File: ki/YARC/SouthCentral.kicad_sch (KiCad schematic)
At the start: 14 parts

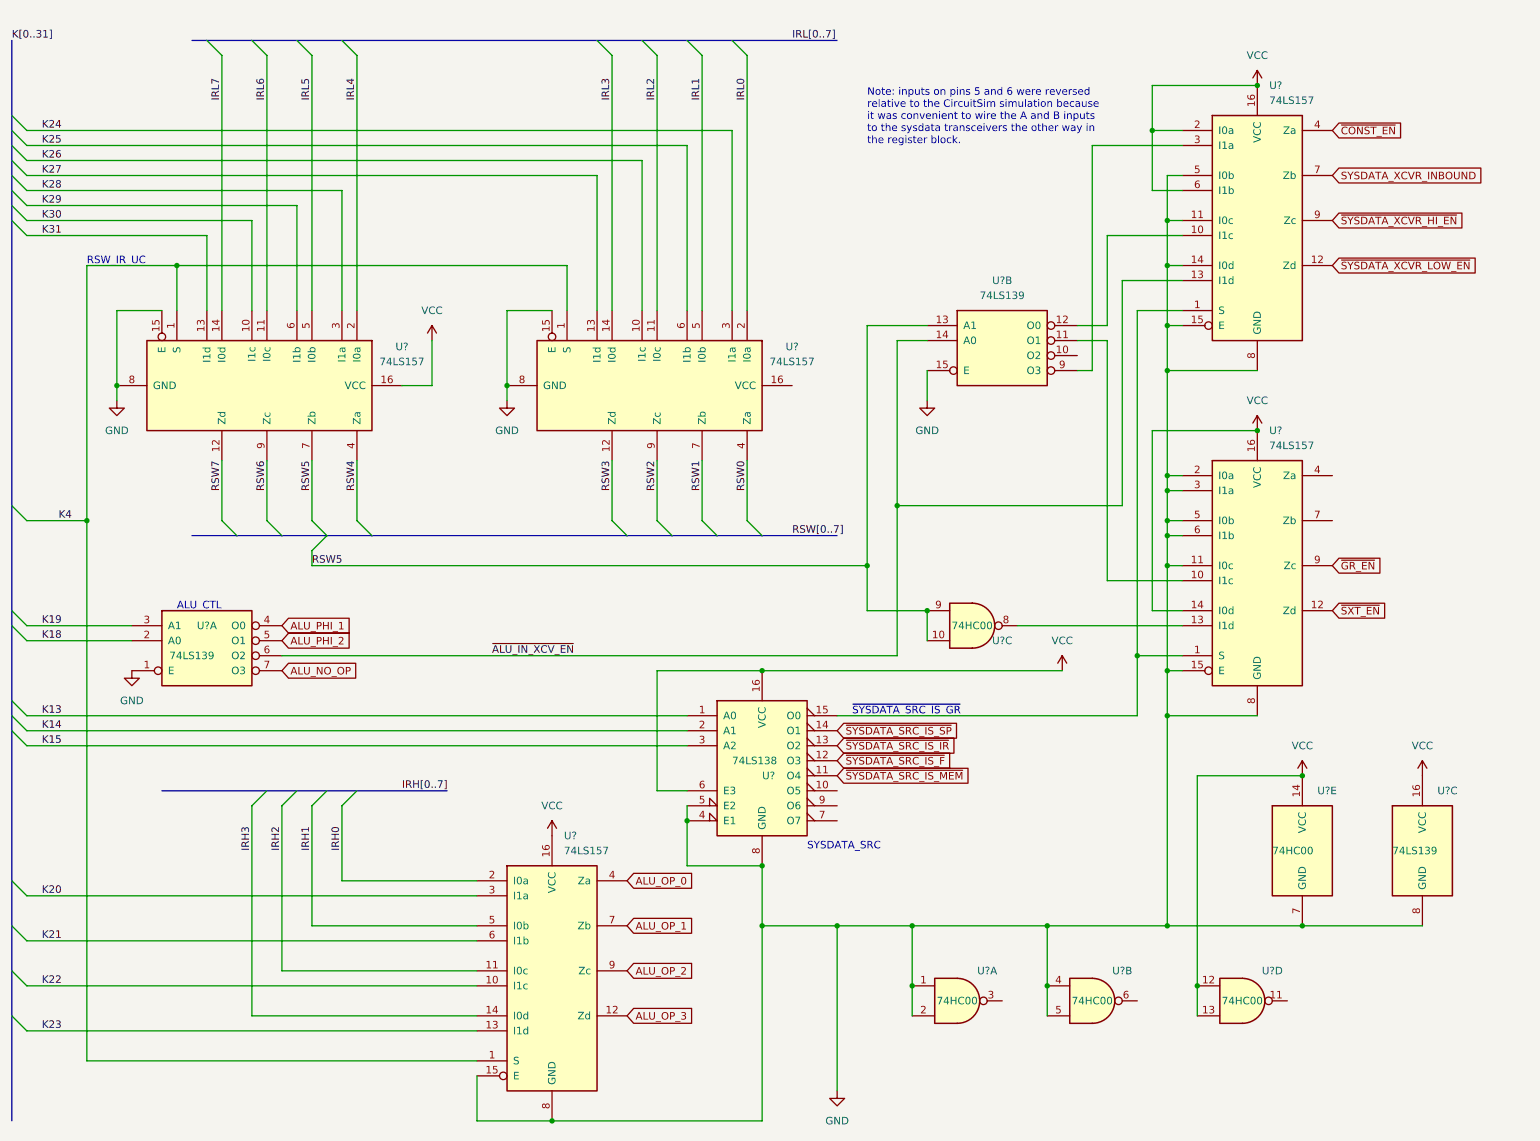
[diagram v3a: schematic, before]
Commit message: Assign part labels (U-numbers) in KiCad and start adding them to Fritzing layouts
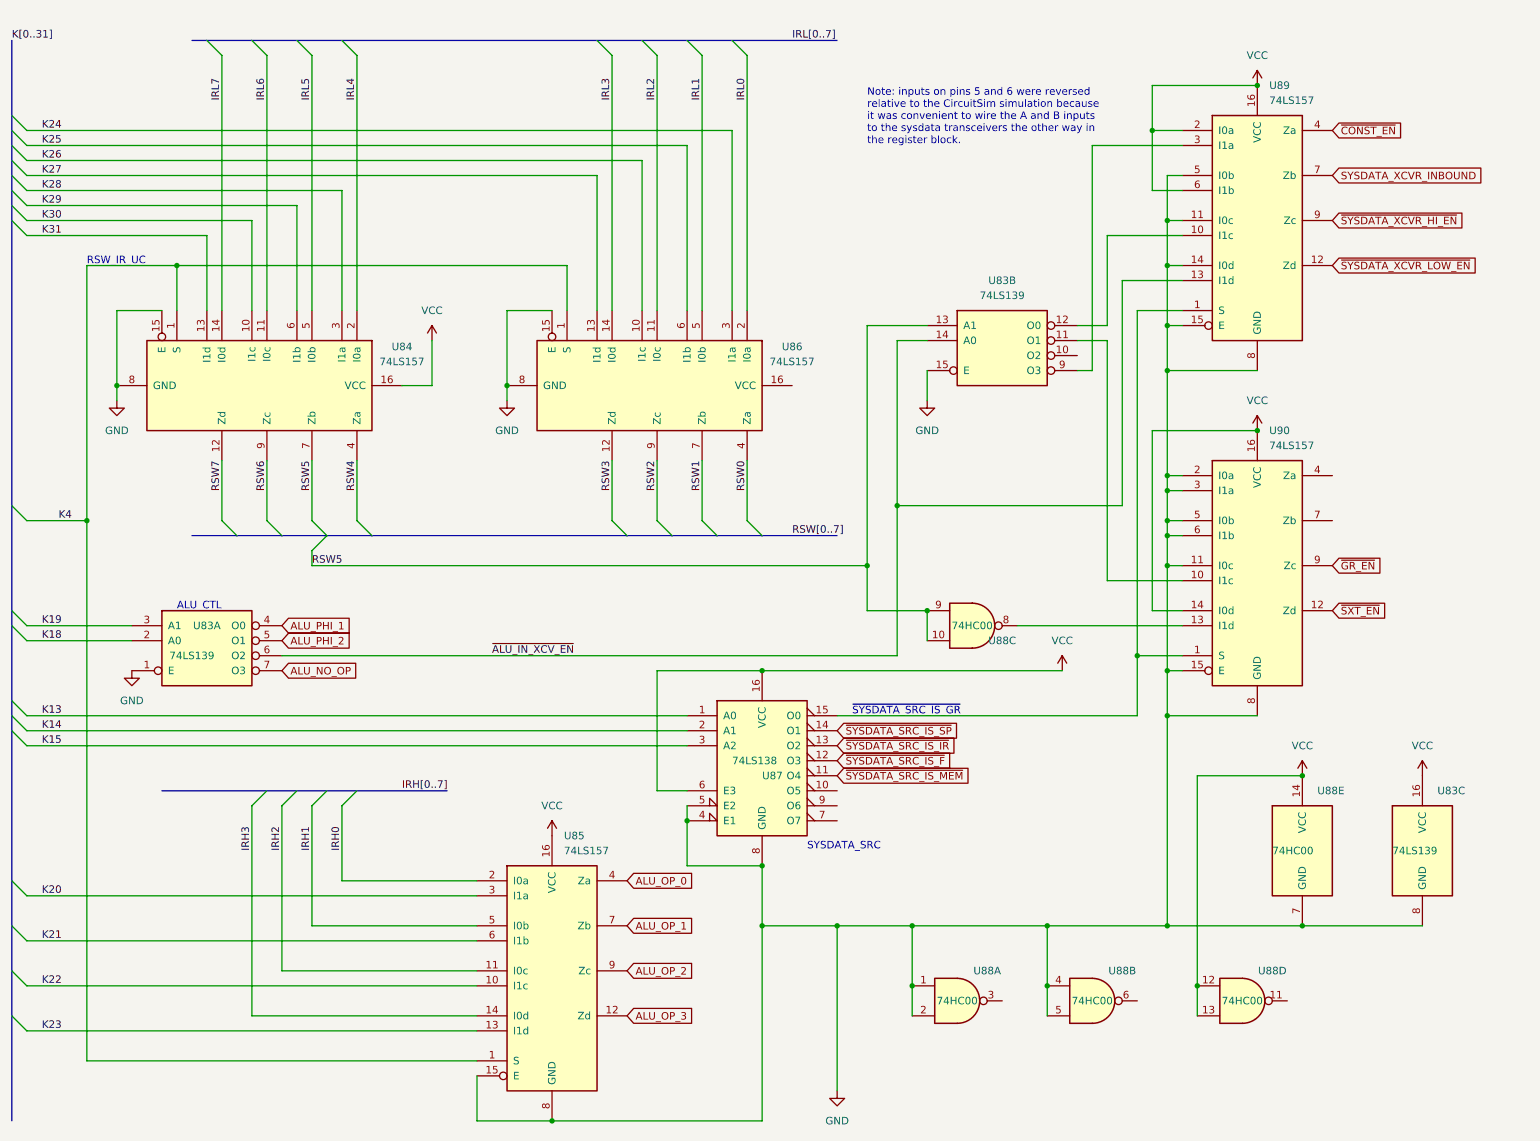
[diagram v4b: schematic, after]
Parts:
- gave numbers to parts that had none: 8
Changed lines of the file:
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@@
   (symbol (lib_id "power:VCC") (at 193.04 124.46 0) (unit 1)
     (in_bom yes) (on_board yes)
-    (property "Reference" "#PWR?" (id 0) (at 193.04 128.27 0)
+    (property "Reference" "#PWR0153" (id 0) (at 193.04 128.27 0)
       (effects (font (size 1.27 1.27)) hide)
     )
@@
   (symbol (lib_id "74xx:74HC00") (at 177.8 116.84 0) (unit 3)
     (in_bom yes) (on_board yes)
-    (property "Reference" "U?" (id 0) (at 182.88 119.38 0))
+    (property "Reference" "U88" (id 0) (at 182.88 119.38 0))
     (property "Value" "74HC00" (id 1) (at 177.8 116.84 0))
     (property "Footprint" "" (id 2) (at 177.8 116.84 0)
@@
   (symbol (lib_id "74xx:74LS139") (at 182.88 68.58 0) (unit 2)
     (in_bom yes) (on_board yes) (fields_autoplaced)
-    (property "Reference" "U?" (id 0) (at 182.88 58.42 0))
+    (property "Reference" "U83" (id 0) (at 182.88 58.42 0))
     (property "Value" "74LS139" (id 1) (at 182.88 60.96 0))
     (property "Footprint" "" (id 2) (at 182.88 68.58 0)
@@
   (symbol (lib_id "power:VCC") (at 86.36 68.58 0) (unit 1)
     (in_bom yes) (on_board yes)
-    (property "Reference" "#PWR?" (id 0) (at 86.36 72.39 0)
+    (property "Reference" "#PWR0148" (id 0) (at 86.36 72.39 0)
       (effects (font (size 1.27 1.27)) hide)
     )
@@
   (symbol (lib_id "74xx:74LS157") (at 226.06 106.68 0) (unit 1)
     (in_bom yes) (on_board yes) (fields_autoplaced)
-    (property "Reference" "U?" (id 0) (at 228.0794 83.82 0)
+    (property "Reference" "U90" (id 0) (at 228.0794 83.82 0)
       (effects (font (size 1.27 1.27)) (justify left))
     )
@@
   (symbol (lib_id "power:VCC") (at 226.06 25.4 0) (unit 1)
     (in_bom yes) (on_board yes) (fields_autoplaced)
-    (property "Reference" "#PWR?" (id 0) (at 226.06 29.21 0)
+    (property "Reference" "#PWR0154" (id 0) (at 226.06 29.21 0)
       (effects (font (size 1.27 1.27)) hide)
     )
@@
   (symbol (lib_id "74xx:74LS157") (at 58.42 76.2 270) (unit 1)
     (in_bom yes) (on_board yes) (fields_autoplaced)
-    (property "Reference" "U?" (id 0) (at 81.28 69.6212 90))
+    (property "Reference" "U84" (id 0) (at 81.28 69.6212 90))
     (property "Value" "74LS157" (id 1) (at 81.28 72.1612 90))
     (property "Footprint" "" (id 2) (at 58.42 76.2 0)
@@
   (symbol (lib_id "power:VCC") (at 106.68 152.4 0) (unit 1)
     (in_bom yes) (on_board yes) (fields_autoplaced)
-    (property "Reference" "#PWR?" (id 0) (at 106.68 156.21 0)
+    (property "Reference" "#PWR0150" (id 0) (at 106.68 156.21 0)
       (effects (font (size 1.27 1.27)) hide)
     )
@@
   (symbol (lib_id "power:GND") (at 35.56 124.46 0) (unit 1)
     (in_bom yes) (on_board yes) (fields_autoplaced)
-    (property "Reference" "#PWR?" (id 0) (at 35.56 130.81 0)
+    (property "Reference" "#PWR0147" (id 0) (at 35.56 130.81 0)
       (effects (font (size 1.27 1.27)) hide)
     )
@@
   (symbol (lib_id "power:GND") (at 33.02 78.74 0) (unit 1)
     (in_bom yes) (on_board yes) (fields_autoplaced)
-    (property "Reference" "#PWR?" (id 0) (at 33.02 85.09 0)
+    (property "Reference" "#PWR0146" (id 0) (at 33.02 85.09 0)
       (effects (font (size 1.27 1.27)) hide)
     )
@@
   (symbol (lib_id "74xx:74HC00") (at 223.52 180.34 0) (unit 4)
     (in_bom yes) (on_board yes)
-    (property "Reference" "U?" (id 0) (at 228.6 175.26 0))
+    (property "Reference" "U88" (id 0) (at 228.6 175.26 0))
     (property "Value" "74HC00" (id 1) (at 223.52 180.34 0))
     (property "Footprint" "" (id 2) (at 223.52 180.34 0)
@@
   (symbol (lib_id "power:GND") (at 154.94 195.58 0) (unit 1)
     (in_bom yes) (on_board yes) (fields_autoplaced)
-    (property "Reference" "#PWR?" (id 0) (at 154.94 201.93 0)
+    (property "Reference" "#PWR0151" (id 0) (at 154.94 201.93 0)
       (effects (font (size 1.27 1.27)) hide)
     )
@@
   (symbol (lib_id "power:VCC") (at 233.68 142.24 0) (unit 1)
     (in_bom yes) (on_board yes) (fields_autoplaced)
-    (property "Reference" "#PWR?" (id 0) (at 233.68 146.05 0)
+    (property "Reference" "#PWR0156" (id 0) (at 233.68 146.05 0)
       (effects (font (size 1.27 1.27)) hide)
     )
@@
   (symbol (lib_id "74xx:74HC00") (at 198.12 180.34 0) (unit 2)
     (in_bom yes) (on_board yes)
-    (property "Reference" "U?" (id 0) (at 203.2 175.26 0))
+    (property "Reference" "U88" (id 0) (at 203.2 175.26 0))
     (property "Value" "74HC00" (id 1) (at 198.12 180.34 0))
     (property "Footprint" "" (id 2) (at 198.12 180.34 0)
@@
   (symbol (lib_id "power:GND") (at 99.06 78.74 0) (unit 1)
     (in_bom yes) (on_board yes) (fields_autoplaced)
-    (property "Reference" "#PWR?" (id 0) (at 99.06 85.09 0)
+    (property "Reference" "#PWR0149" (id 0) (at 99.06 85.09 0)
       (effects (font (size 1.27 1.27)) hide)
     )
@@
   (symbol (lib_id "74xx:74LS139") (at 48.26 119.38 0) (unit 1)
     (in_bom yes) (on_board yes)
-    (property "Reference" "U?" (id 0) (at 48.26 116.84 0))
+    (property "Reference" "U83" (id 0) (at 48.26 116.84 0))
     (property "Value" "74LS139" (id 1) (at 45.72 121.92 0))
     (property "Footprint" "" (id 2) (at 48.26 119.38 0)
@@
   (symbol (lib_id "power:GND") (at 170.18 78.74 0) (unit 1)
     (in_bom yes) (on_board yes) (fields_autoplaced)
-    (property "Reference" "#PWR?" (id 0) (at 170.18 85.09 0)
+    (property "Reference" "#PWR0152" (id 0) (at 170.18 85.09 0)
       (effects (font (size 1.27 1.27)) hide)
     )
@@
   (symbol (lib_id "74xx:74LS138") (at 142.24 139.7 0) (unit 1)
     (in_bom yes) (on_board yes)
-    (property "Reference" "U?" (id 0) (at 142.24 142.24 0)
+    (property "Reference" "U87" (id 0) (at 142.24 142.24 0)
       (effects (font (size 1.27 1.27)) (justify left))
     )
@@
   (symbol (lib_id "power:VCC") (at 226.06 83.82 0) (unit 1)
     (in_bom yes) (on_board yes) (fields_autoplaced)
-    (property "Reference" "#PWR?" (id 0) (at 226.06 87.63 0)
+    (property "Reference" "#PWR0155" (id 0) (at 226.06 87.63 0)
       (effects (font (size 1.27 1.27)) hide)
     )
@@
   (symbol (lib_id "74xx:74HC00") (at 175.26 180.34 0) (unit 1)
     (in_bom yes) (on_board yes)
-    (property "Reference" "U?" (id 0) (at 180.34 175.26 0))
+    (property "Reference" "U88" (id 0) (at 180.34 175.26 0))
     (property "Value" "74HC00" (id 1) (at 175.26 180.34 0))
     (property "Footprint" "" (id 2) (at 175.26 180.34 0)
@@
   (symbol (lib_id "74xx:74LS157") (at 106.68 175.26 0) (unit 1)
     (in_bom yes) (on_board yes) (fields_autoplaced)
-    (property "Reference" "U?" (id 0) (at 108.6994 152.4 0)
+    (property "Reference" "U85" (id 0) (at 108.6994 152.4 0)
       (effects (font (size 1.27 1.27)) (justify left))
     )
@@
   (symbol (lib_id "74xx:74LS157") (at 226.06 48.26 0) (unit 1)
     (in_bom yes) (on_board yes) (fields_autoplaced)
-    (property "Reference" "U?" (id 0) (at 228.0794 25.4 0)
+    (property "Reference" "U89" (id 0) (at 228.0794 25.4 0)
       (effects (font (size 1.27 1.27)) (justify left))
     )
@@
   (symbol (lib_id "74xx:74LS139") (at 254 154.94 0) (unit 3)
     (in_bom yes) (on_board yes)
-    (property "Reference" "U?" (id 0) (at 256.54 144.78 0)
+    (property "Reference" "U83" (id 0) (at 256.54 144.78 0)
       (effects (font (size 1.27 1.27)) (justify left))
     )
@@
   (symbol (lib_id "74xx:74LS157") (at 124.46 76.2 270) (unit 1)
     (in_bom yes) (on_board yes) (fields_autoplaced)
-    (property "Reference" "U?" (id 0) (at 147.32 69.6212 90))
+    (property "Reference" "U86" (id 0) (at 147.32 69.6212 90))
     (property "Value" "74LS157" (id 1) (at 147.32 72.1612 90))
     (property "Footprint" "" (id 2) (at 124.46 76.2 0)
@@
   (symbol (lib_id "74xx:74HC00") (at 233.68 154.94 0) (unit 5)
     (in_bom yes) (on_board yes)
-    (property "Reference" "U?" (id 0) (at 236.22 144.78 0)
+    (property "Reference" "U88" (id 0) (at 236.22 144.78 0)
       (effects (font (size 1.27 1.27)) (justify left))
     )
@@
   (symbol (lib_id "power:VCC") (at 254 142.24 0) (unit 1)
     (in_bom yes) (on_board yes) (fields_autoplaced)
-    (property "Reference" "#PWR?" (id 0) (at 254 146.05 0)
-      (effects (font (size 1.27 1.27)) hide)
-    )
+    (property "Reference" "#PWR0157" (id 0) (at 254 146.05 0)
+      (effects (font (size 1.27 1.27)) hide)
+    )

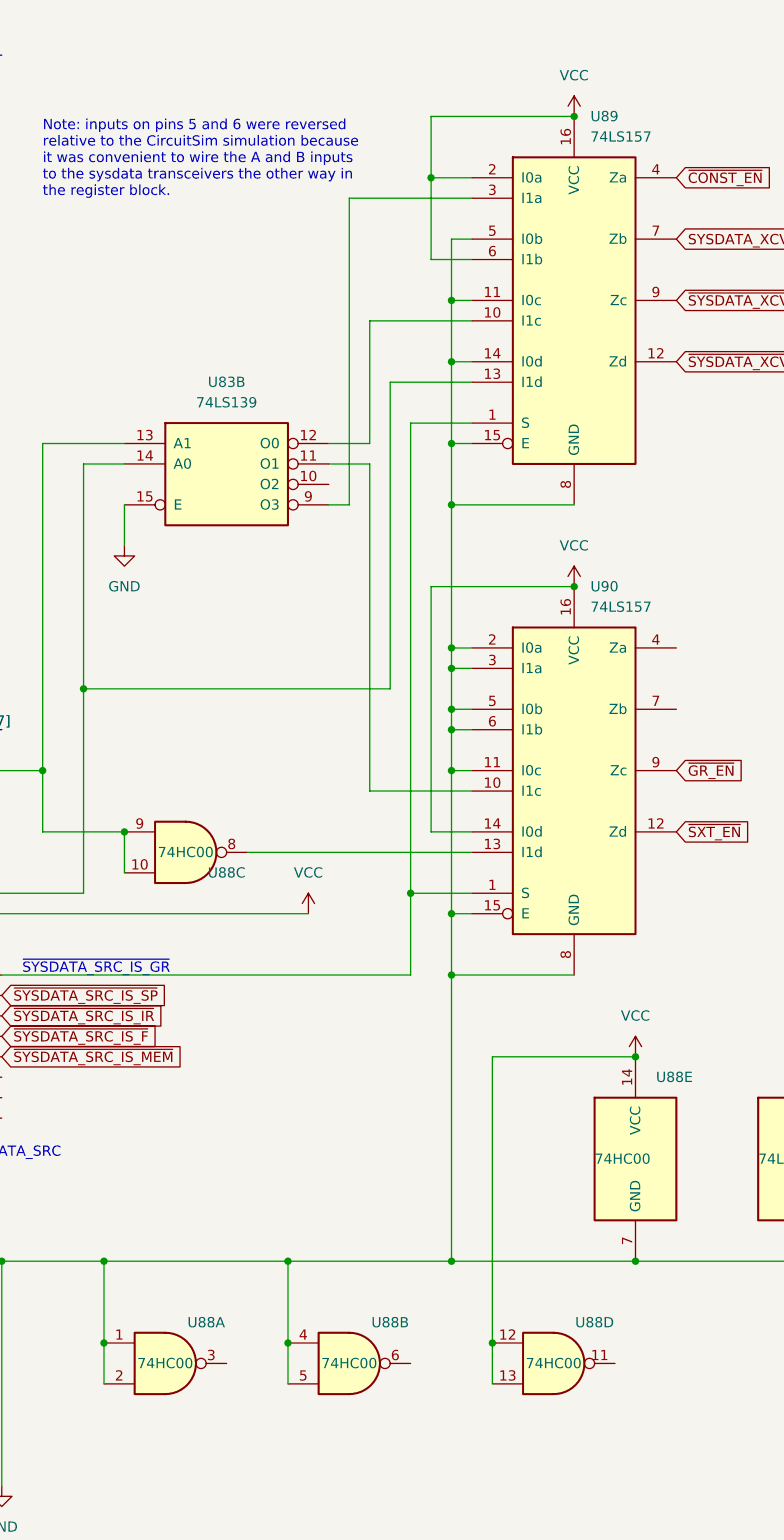
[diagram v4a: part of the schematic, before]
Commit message: Continue annotating and labeling ICs
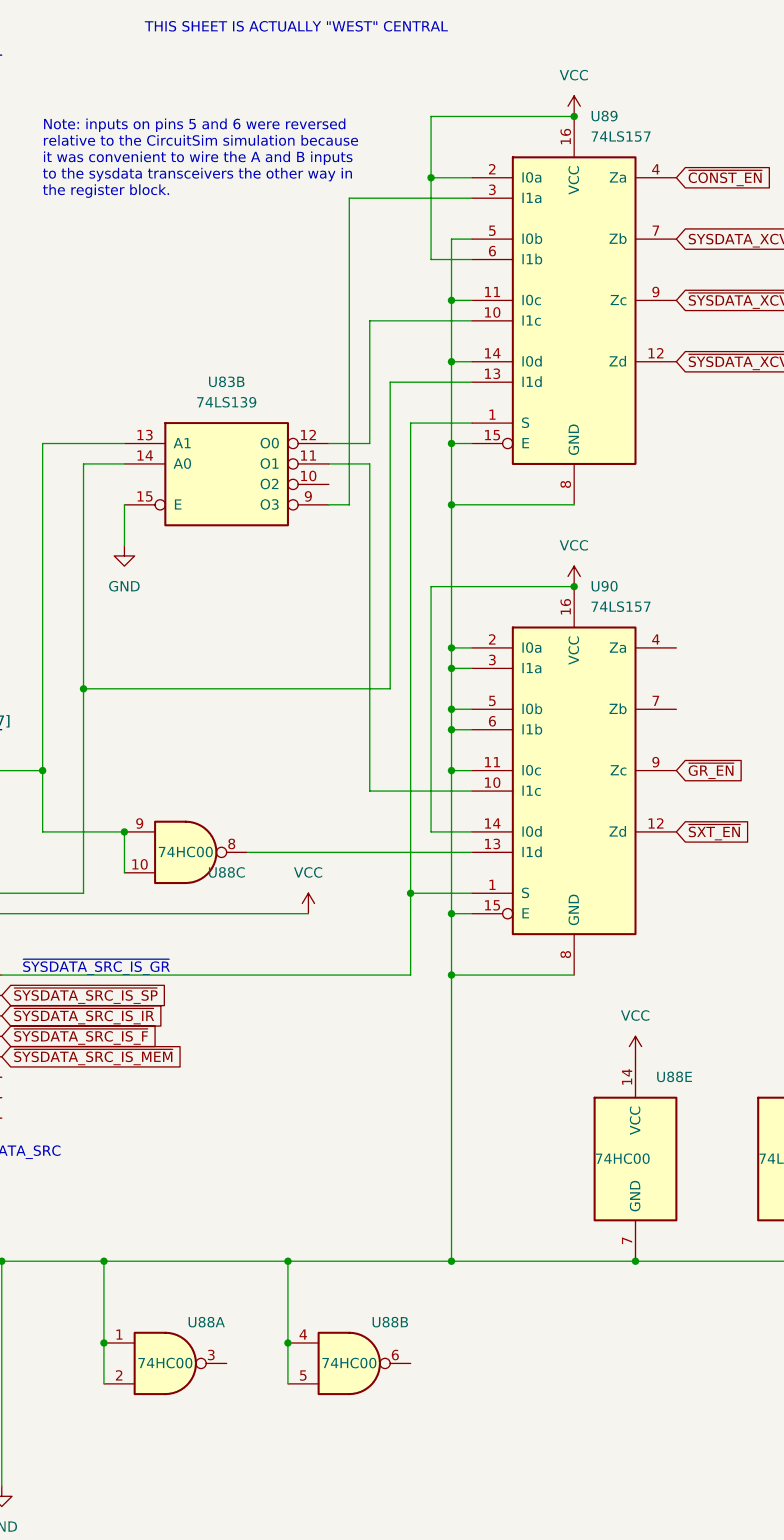
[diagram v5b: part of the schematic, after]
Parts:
- removed unit 4 of U88
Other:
- note added: "THIS SHEET IS ACTUALLY "WEST" CENTRAL"
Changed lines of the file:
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@@
   (junction (at 190.5 167.64) (diameter 0) (color 0 0 0 0)
   )
-  (junction (at 215.9 177.8) (diameter 0) (color 0 0 0 0)
-  )
   (junction (at 210.82 93.98) (diameter 0) (color 0 0 0 0)
   )
@@
   (junction (at 226.06 25.4) (diameter 0) (color 0 0 0 0)
   )
-  (junction (at 233.68 142.24) (diameter 0) (color 0 0 0 0)
-  )
   (junction (at 190.5 177.8) (diameter 0) (color 0 0 0 0)
   )
@@
     (stroke (width 0) (type default) (color 0 0 0 0))
   )
-  (wire (pts (xy 215.9 142.24) (xy 233.68 142.24))
-    (stroke (width 0) (type default) (color 0 0 0 0))
-  )
   (wire (pts (xy 200.66 50.8) (xy 213.36 50.8))
     (stroke (width 0) (type default) (color 0 0 0 0))
@@
     (stroke (width 0) (type default) (color 0 0 0 0))
   )
-  (wire (pts (xy 215.9 182.88) (xy 215.9 177.8))
-    (stroke (width 0) (type default) (color 0 0 0 0))
-  )
   (wire (pts (xy 60.96 121.92) (xy 165.1 121.92))
     (stroke (width 0) (type default) (color 0 0 0 0))
@@
     (stroke (width 0) (type default) (color 0 0 0 0))
   )
-  (wire (pts (xy 215.9 177.8) (xy 215.9 142.24))
-    (stroke (width 0) (type default) (color 0 0 0 0))
-  )
   (bus (pts (xy 40.64 144.78) (xy 58.42 144.78))
     (stroke (width 0) (type default) (color 0 0 0 0))
@@
   )
   (text "RSW_IR_UC" (at 27.94 55.88 0)
+    (effects (font (size 1.27 1.27)) (justify left bottom))
+  )
+  (text "THIS SHEET IS ACTUALLY \"WEST\" CENTRAL" (at 172.72 15.24 0)
     (effects (font (size 1.27 1.27)) (justify left bottom))
   )
@@
     (pin "1")
   )
-  (symbol (lib_id "74xx:74HC00") (at 223.52 180.34 0) (unit 4)
-    (in_bom yes) (on_board yes)
-    (property "Reference" "U88" (id 0) (at 228.6 175.26 0))
-    (property "Value" "74HC00" (id 1) (at 223.52 180.34 0))
-    (property "Footprint" "" (id 2) (at 223.52 180.34 0)
-      (effects (font (size 1.27 1.27)) hide)
-    )
-    (property "Datasheet" "http://www.ti.com/lit/gpn/sn74hc00" (id 3) (at 223.52 180.34 0)
-      (effects (font (size 1.27 1.27)) hide)
-    )
-    (pin "11")
-    (pin "12")
-    (pin "13")
-  )
   (symbol (lib_id "power:GND") (at 154.94 195.58 0) (unit 1)
